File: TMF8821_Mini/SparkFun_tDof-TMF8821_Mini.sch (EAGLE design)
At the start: 29 parts, among them J4 QWIIC_RIGHT_ANGLE, J5 QWIIC_RIGHT_ANGLE

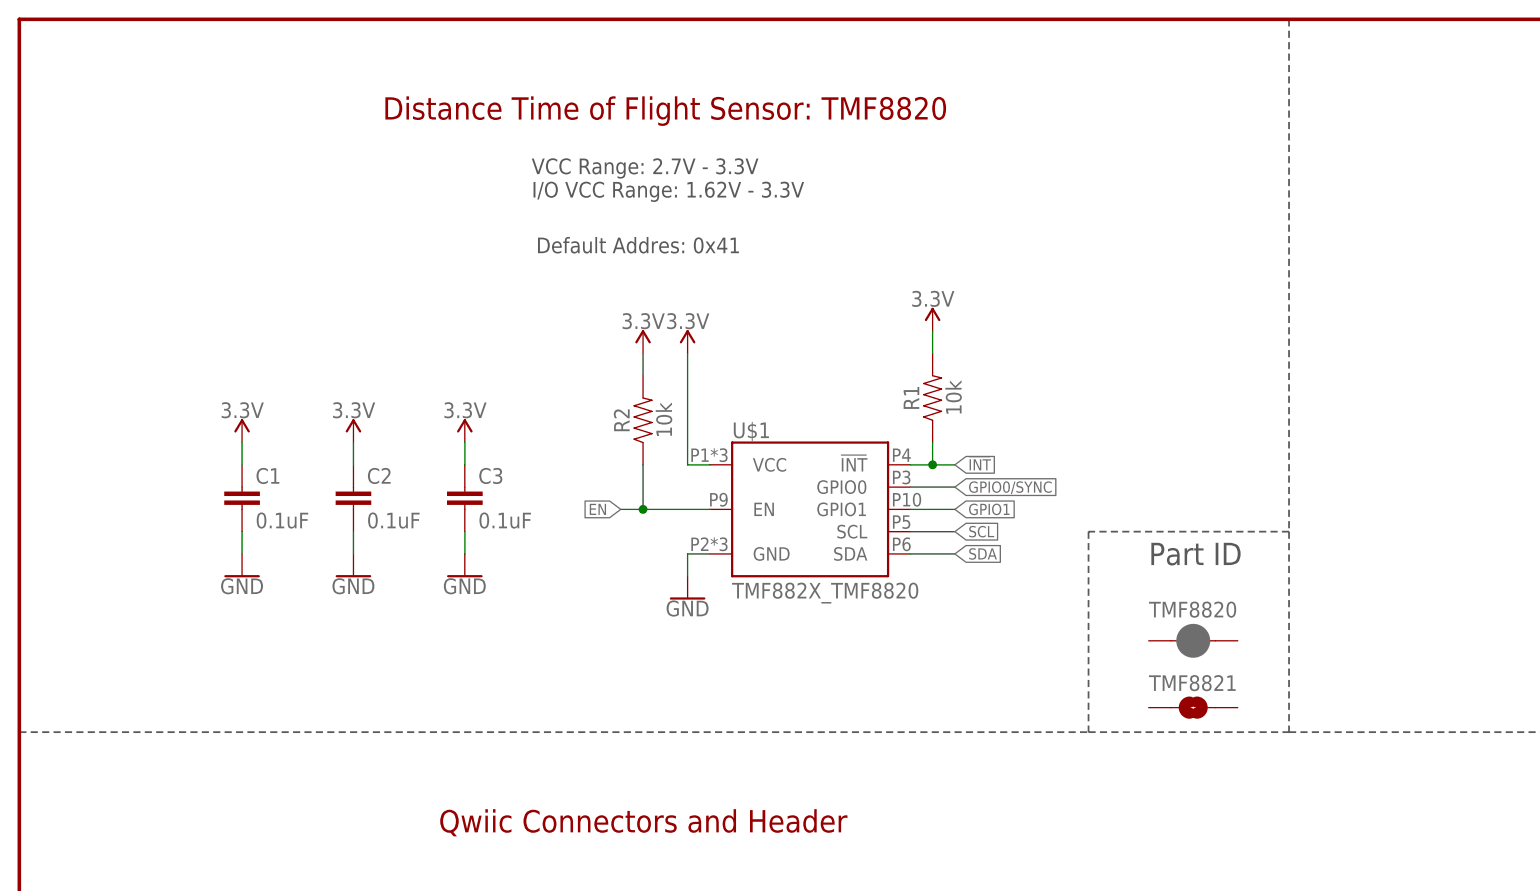
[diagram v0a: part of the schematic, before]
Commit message: Removes old production files
* Removes old 8821 "HQ" variants
* Copies the 8820 and 8820 Mini variants
* Adjusts new 8820 copies to reference 8821 and replaces 8820 with 8821
* Updates Product Identifier jumpers to reflect changes
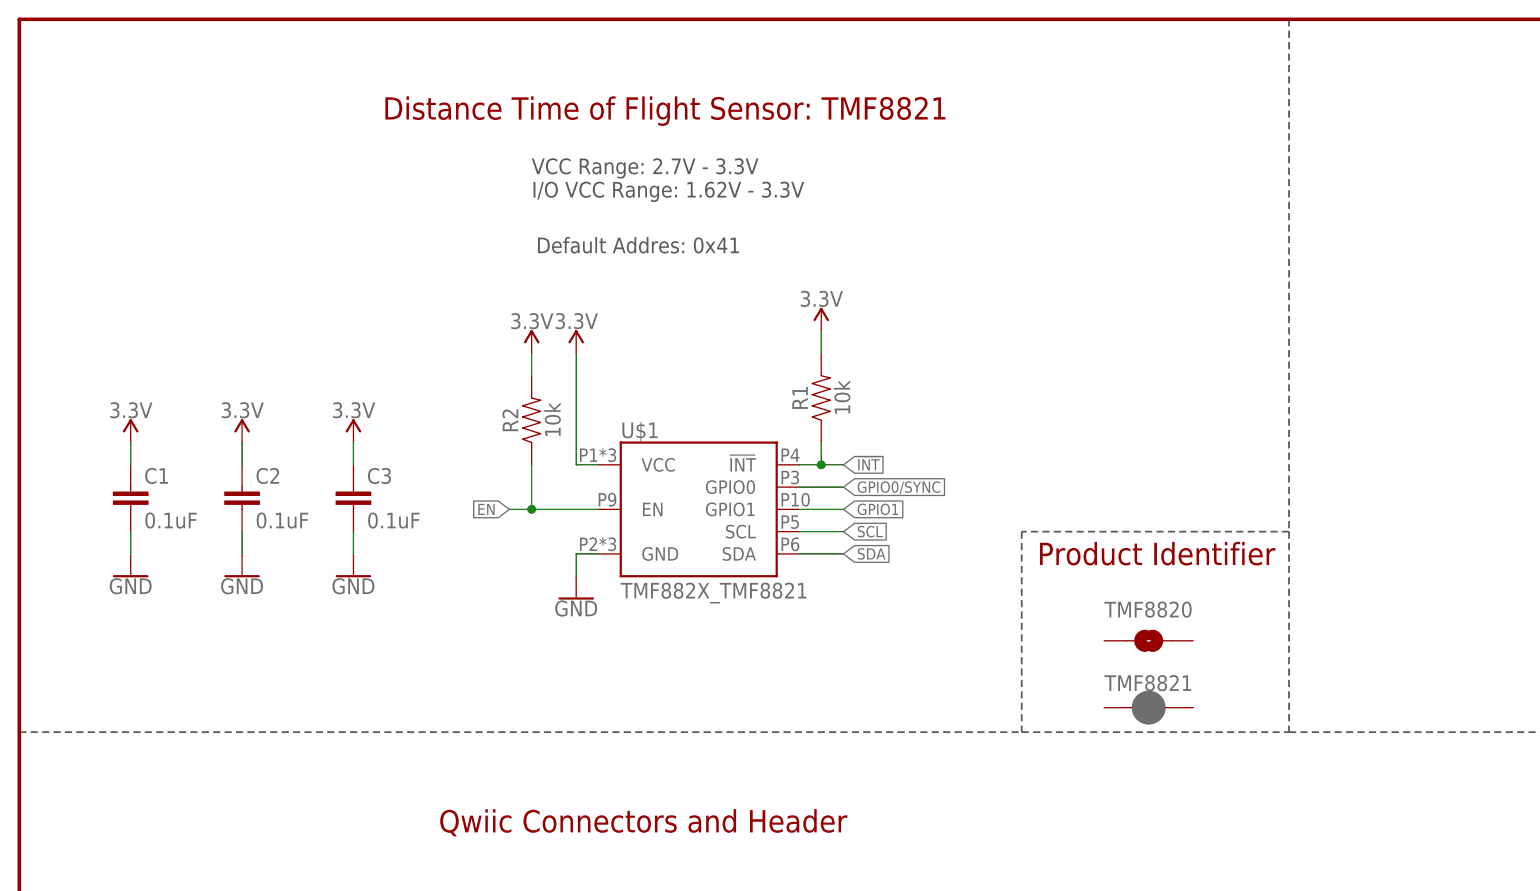
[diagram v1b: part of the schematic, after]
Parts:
- TMF8820: value JUMPER-SMT_2_NC_PASTE_SILK -> JUMPER-SMT_2_NO_SILK; device SparkFun-Jumpers:JUMPER-SMT_2_NC_PASTE_SILK -> SparkFun-Jumpers:JUMPER-SMT_2_NO_SILK
- TMF8821: value JUMPER-SMT_2_NO_SILK -> JUMPER-SMT_2_NC_PASTE_SILK; device SparkFun-Jumpers:JUMPER-SMT_2_NO_SILK -> SparkFun-Jumpers:JUMPER-SMT_2_NC_PASTE_SILK
- U$1: value TMF882X_TMF8820 -> TMF882X_TMF8821; device TMF882X:TMF882X_TMF8820 -> TMF882X:TMF882X_TMF8821
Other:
- note added: "Distance Time of Flight Sensor: TMF8821"
- note added: "Product Identifier"
- note removed: "Distance Time of Flight Sensor: TMF8820"
- note removed: "Part ID"
- moved on the sheet: C1, C2, C3, R1, R2, U$1

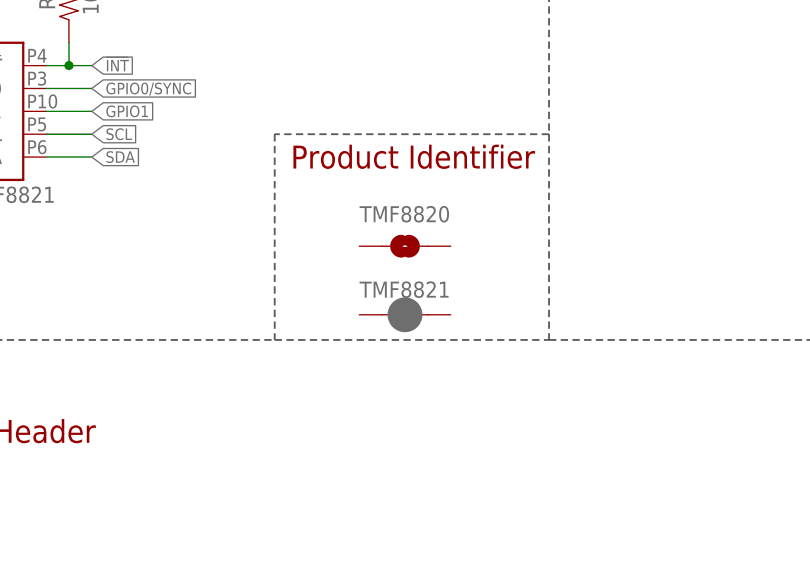
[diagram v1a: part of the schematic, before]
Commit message: Adds new product identifier pads to all designs, rolls 8820 version number to v10
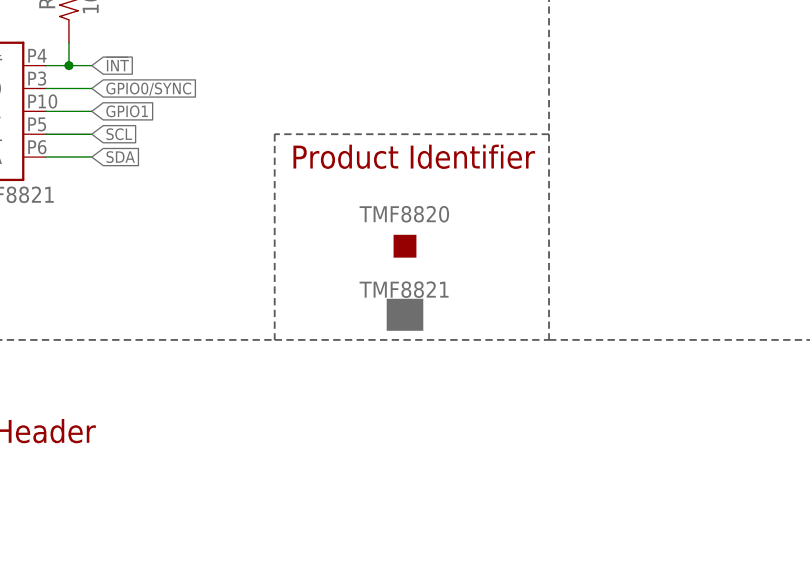
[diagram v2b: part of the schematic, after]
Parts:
- TMF8820: value JUMPER-SMT_2_NO_SILK -> PROD_ID_NO-PASTE_SILK; device SparkFun-Jumpers:JUMPER-SMT_2_NO_SILK -> SparkFun-Aesthetics:PROD_ID_NO-PASTE_SILK
- TMF8821: value JUMPER-SMT_2_NC_PASTE_SILK -> PROD_ID_PASTE_SILK; device SparkFun-Jumpers:JUMPER-SMT_2_NC_PASTE_SILK -> SparkFun-Aesthetics:PROD_ID_PASTE_SILK
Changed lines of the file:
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@@
 <part name="LOGO2" library="SparkFun-Aesthetics" deviceset="QWIIC_LOGO" device="_3MM"/>
 <part name="LOGO3" library="SparkFun-Aesthetics" deviceset="OSHW-LOGO" device="NO_SILK"/>
-<part name="TMF8820" library="SparkFun-Jumpers" deviceset="JUMPER-SMT_2_NO" device="_SILK" package3d_urn="urn:adsk.eagle:package:39279/1"/>
-<part name="TMF8821" library="SparkFun-Jumpers" deviceset="JUMPER-SMT_2_NC_PASTE" device="_SILK" package3d_urn="urn:adsk.eagle:package:39282/1"/>
+<part name="TMF8820" library="SparkFun-Aesthetics" deviceset="PROD_ID_NO-PASTE" device="_SILK"/>
+<part name="TMF8821" library="SparkFun-Aesthetics" deviceset="PROD_ID_PASTE" device="_SILK"/>
 </parts>
 <sheets>

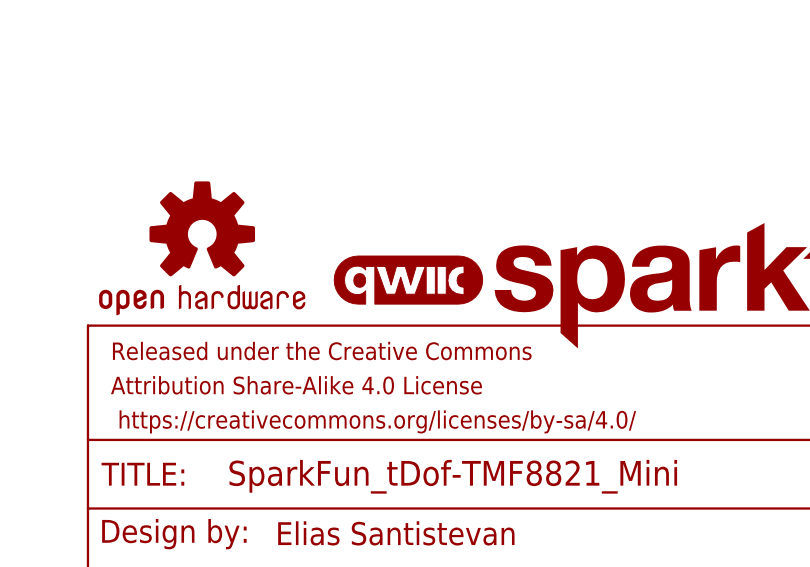
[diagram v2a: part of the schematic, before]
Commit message: Changes all "IO" silk to be "GP" instead, increases Qwiic pill size on mini's
* Fixes orientation of I2C and LED silk on mini versions
* Increases SparkFun flame size on mini versions
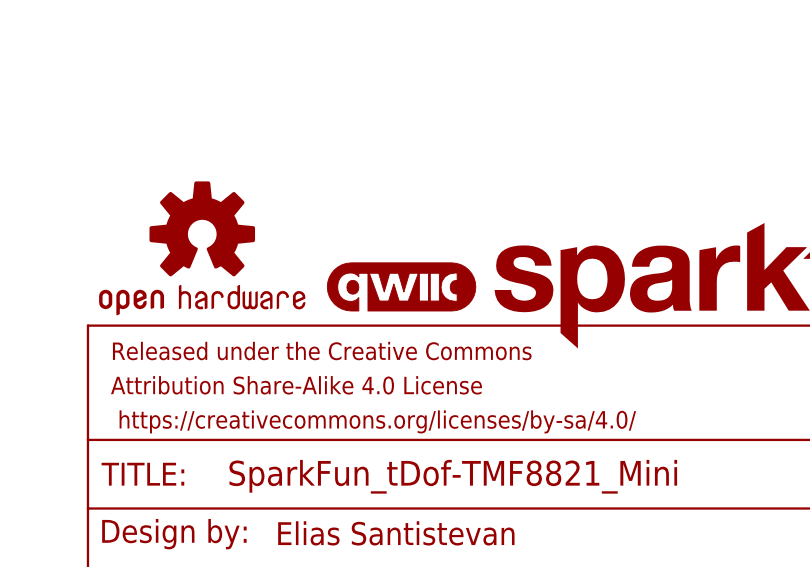
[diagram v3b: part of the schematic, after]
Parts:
- LOGO2: value QWIIC_LOGO_3MM -> QWIIC_LOGO_4MM; device SparkFun-Aesthetics:QWIIC_LOGO_3MM -> SparkFun-Aesthetics:QWIIC_LOGO_4MM
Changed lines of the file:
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@@
 <part name="J3" library="SparkFun-Connectors" deviceset="CONN_02" device="1X02_NO_SILK"/>
 <part name="LOGO1" library="SparkFun-Aesthetics" deviceset="SFE_LOGO_NAME" device="BLANK"/>
-<part name="LOGO2" library="SparkFun-Aesthetics" deviceset="QWIIC_LOGO" device="_3MM"/>
 <part name="LOGO3" library="SparkFun-Aesthetics" deviceset="OSHW-LOGO" device="NO_SILK"/>
 <part name="TMF8820" library="SparkFun-Aesthetics" deviceset="PROD_ID_NO-PASTE" device="_SILK"/>
 <part name="TMF8821" library="SparkFun-Aesthetics" deviceset="PROD_ID_PASTE" device="_SILK"/>
+<part name="LOGO2" library="SparkFun-Aesthetics" deviceset="QWIIC_LOGO" device="_4MM"/>
 </parts>
 <sheets>
@@
 </instance>
 <instance part="LOGO1" gate="G$1" x="190.5" y="33.02" smashed="yes"/>
-<instance part="LOGO2" gate="G$1" x="182.88" y="40.64" smashed="yes"/>
 <instance part="LOGO3" gate="G$1" x="160.02" y="45.72" smashed="yes"/>
 <instance part="TMF8820" gate="G$1" x="128.778" y="114.554" smashed="yes">
@@
 <attribute name="NAME" x="128.778" y="109.728" size="1.778" layer="95" font="vector" align="center"/>
 </instance>
+<instance part="LOGO2" gate="G$1" x="182.118" y="39.878" smashed="yes"/>
 </instances>
 <busses>
